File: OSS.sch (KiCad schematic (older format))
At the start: 2 parts, among them U5 27C128

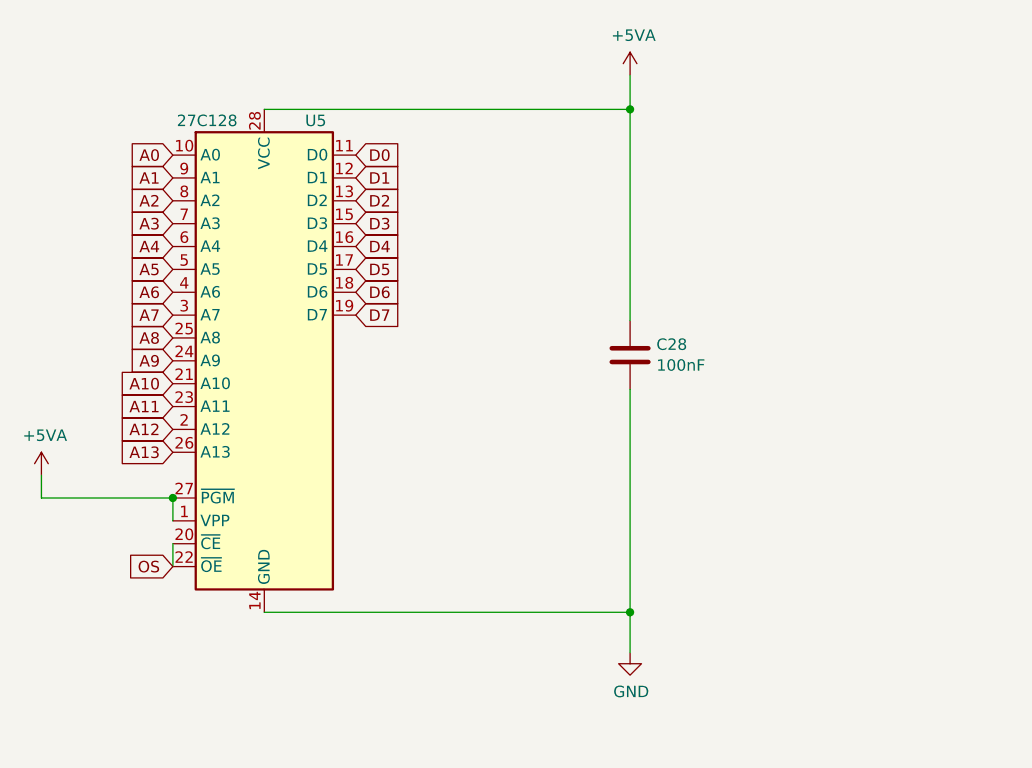
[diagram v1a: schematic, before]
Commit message: OSS and Basic in PLCC
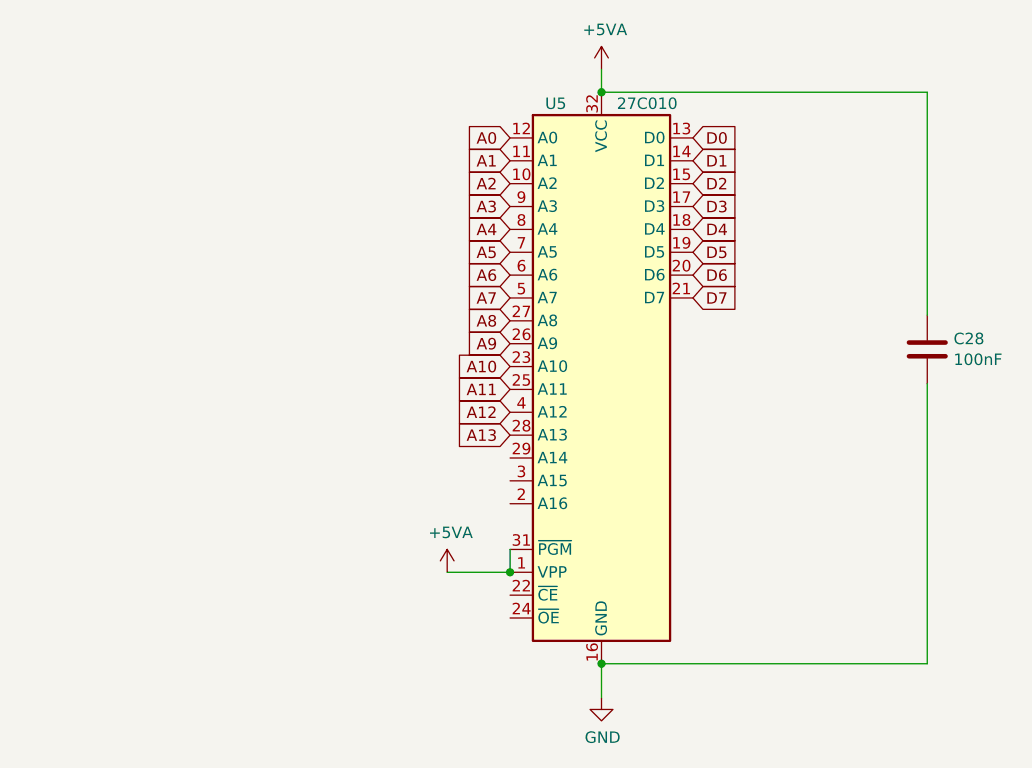
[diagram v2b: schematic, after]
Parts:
- removed U5: 27C128, Package_DIP:DIP-28_W15.24mm_Socket, symbol Memory_EPROM:27C128
- added U5: 27C010, Atari:PLCC-32_THT-Socket, symbol Memory_EPROM:27C010
- C28: footprint Atari:C_Axial_L5.1mm_D2.5mm_P12.50mm_Horizontal -> Capacitor_SMD:C_1206_3216Metric_Pad1.42x1.75mm_HandSolder
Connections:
- net +5VA: now also U5.1 (VPP), U5.31 (~PGM), U5.32 (VCC)
- net A0: now also U5.12 (A0)
- net A1: now also U5.11 (A1)
- net A10: now also U5.23 (A10)
- net A11: now also U5.25 (A11)
- net A12: now also U5.4 (A12)
- net A13: now also U5.28 (A13)
- net A2: now also U5.10 (A2)
- net A3: now also U5.9 (A3)
- net A4: now also U5.8 (A4)
- net A5: now also U5.7 (A5)
- net A6: now also U5.6 (A6)
- net A7: now also U5.5 (A7)
- net A8: now also U5.27 (A8)
- net A9: now also U5.26 (A9)
- net D0: now also U5.13 (D0)
- net D1: now also U5.14 (D1)
- net D2: now also U5.15 (D2)
- net D3: now also U5.17 (D3)
- net D4: now also U5.18 (D4)
- net D5: now also U5.19 (D5)
- net D6: now also U5.20 (D6)
- net D7: now also U5.21 (D7)
- net GND: now also U5.16 (GND)
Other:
- moved on the sheet: C28
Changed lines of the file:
@@
 Comment4 ""
 $EndDescr
-$Comp
-L Memory_EPROM:27C128 U5
-U 1 1 6021796E
-P 5650 3850
-F 0 "U5" H 5875 4900 50  0000 C CNN
-F 1 "27C128" H 5400 4900 50  0000 C CNN
-F 2 "Package_DIP:DIP-28_W15.24mm_Socket" H 5650 3850 50  0001 C CNN
-F 3 "http://ww1.microchip.com/downloads/en/devicedoc/11003L.pdf" H 5650 3850 50  0001 C CNN
-	1    5650 3850
-	1    0    0    -1
-$EndComp
-Text GLabel 5250 2950 0    50   Input ~ 0
+Text GLabel 6725 2875 0    50   Input ~ 0
 A0
-Text GLabel 5250 3050 0    50   Input ~ 0
+Text GLabel 6725 2975 0    50   Input ~ 0
 A1
-Text GLabel 5250 3150 0    50   Input ~ 0
+Text GLabel 6725 3075 0    50   Input ~ 0
 A2
-Text GLabel 5250 3250 0    50   Input ~ 0
+Text GLabel 6725 3175 0    50   Input ~ 0
 A3
-Text GLabel 5250 3350 0    50   Input ~ 0
+Text GLabel 6725 3275 0    50   Input ~ 0
 A4
-Text GLabel 5250 3450 0    50   Input ~ 0
+Text GLabel 6725 3375 0    50   Input ~ 0
 A5
-Text GLabel 5250 3550 0    50   Input ~ 0
+Text GLabel 6725 3475 0    50   Input ~ 0
 A6
-Text GLabel 5250 3650 0    50   Input ~ 0
+Text GLabel 6725 3575 0    50   Input ~ 0
 A7
-Text GLabel 5250 3750 0    50   Input ~ 0
+Text GLabel 6725 3675 0    50   Input ~ 0
 A8
-Text GLabel 5250 3850 0    50   Input ~ 0
+Text GLabel 6725 3775 0    50   Input ~ 0
 A9
-Text GLabel 5250 3950 0    50   Input ~ 0
+Text GLabel 6725 3875 0    50   Input ~ 0
 A10
-Text GLabel 5250 4050 0    50   Input ~ 0
+Text GLabel 6725 3975 0    50   Input ~ 0
 A11
-Text GLabel 5250 4150 0    50   Input ~ 0
+Text GLabel 6725 4075 0    50   Input ~ 0
 A12
-Text GLabel 5250 4250 0    50   Input ~ 0
+Text GLabel 6725 4175 0    50   Input ~ 0
 A13
-Wire Wire Line
-	5250 4450 5250 4550
-Wire Wire Line
-	5250 4650 5250 4750
-Text GLabel 5250 4750 0    50   Input ~ 0
-OS
 $Comp
 L power:+5VA #PWR0149
 U 1 1 60218ED9
-P 4675 4350
-F 0 "#PWR0149" H 4675 4200 50  0001 C CNN
-F 1 "+5VA" H 4690 4523 50  0000 C CNN
-F 2 "" H 4675 4350 50  0001 C CNN
-F 3 "" H 4675 4350 50  0001 C CNN
-	1    4675 4350
+P 6450 4775
+F 0 "#PWR0149" H 6450 4625 50  0001 C CNN
+F 1 "+5VA" H 6465 4948 50  0000 C CNN
+F 2 "" H 6450 4775 50  0001 C CNN
+F 3 "" H 6450 4775 50  0001 C CNN
+	1    6450 4775
 	1    0    0    -1
 $EndComp
-Wire Wire Line
-	5250 4450 4675 4450
-Wire Wire Line
-	4675 4450 4675 4350
-Connection ~ 5250 4450
-Text GLabel 6050 2950 2    50   Input ~ 0
+Text GLabel 7525 2875 2    50   Input ~ 0
 D0
-Text GLabel 6050 3050 2    50   Input ~ 0
+Text GLabel 7525 2975 2    50   Input ~ 0
 D1
-Text GLabel 6050 3150 2    50   Input ~ 0
+Text GLabel 7525 3075 2    50   Input ~ 0
 D2
-Text GLabel 6050 3250 2    50   Input ~ 0
+Text GLabel 7525 3175 2    50   Input ~ 0
 D3
-Text GLabel 6050 3350 2    50   Input ~ 0
+Text GLabel 7525 3275 2    50   Input ~ 0
 D4
-Text GLabel 6050 3450 2    50   Input ~ 0
+Text GLabel 7525 3375 2    50   Input ~ 0
 D5
-Text GLabel 6050 3550 2    50   Input ~ 0
+Text GLabel 7525 3475 2    50   Input ~ 0
 D6
-Text GLabel 6050 3650 2    50   Input ~ 0
+Text GLabel 7525 3575 2    50   Input ~ 0
 D7
 $Comp
 L Device:C C28
 U 1 1 6021A354
-P 7250 3825
-F 0 "C28" H 7365 3871 50  0000 L CNN
-F 1 "100nF" H 7365 3780 50  0000 L CNN
-F 2 "Atari:C_Axial_L5.1mm_D2.5mm_P12.50mm_Horizontal" H 7288 3675 50  0001 C CNN
-F 3 "~" H 7250 3825 50  0001 C CNN
-	1    7250 3825
+P 8550 3800
+F 0 "C28" H 8665 3846 50  0000 L CNN
+F 1 "100nF" H 8665 3755 50  0000 L CNN
+F 2 "Capacitor_SMD:C_1206_3216Metric_Pad1.42x1.75mm_HandSolder" H 8588 3650 50  0001 C CNN
+F 3 "~" H 8550 3800 50  0001 C CNN
+	1    8550 3800
+	1    0    0    -1
+$EndComp
+$Comp
+L power:+5VA #PWR0150
+U 1 1 6021B092
+P 7125 2575
+F 0 "#PWR0150" H 7125 2425 50  0001 C CNN
+F 1 "+5VA" H 7140 2748 50  0000 C CNN
+F 2 "" H 7125 2575 50  0001 C CNN
+F 3 "" H 7125 2575 50  0001 C CNN
+	1    7125 2575
+	1    0    0    -1
+$EndComp
+$Comp
+L power:GND #PWR0151
+U 1 1 6021B848
+P 7125 5325
+F 0 "#PWR0151" H 7125 5075 50  0001 C CNN
+F 1 "GND" H 7130 5152 50  0000 C CNN
+F 2 "" H 7125 5325 50  0001 C CNN
+F 3 "" H 7125 5325 50  0001 C CNN
+	1    7125 5325
+	1    0    0    -1
+$EndComp
+$Comp
+L Memory_EPROM:27C010 U5
+U 1 1 60AAC553
+P 7125 3875
+F 0 "U5" H 6925 5025 50  0000 C CNN
+F 1 "27C010" H 7325 5025 50  0000 C CNN
+F 2 "Atari:PLCC-32_THT-Socket" H 7125 3875 50  0001 C CNN
+F 3 "http://ww1.microchip.com/downloads/en/DeviceDoc/doc0321.pdf" H 7125 3875 50  0001 C CNN
+	1    7125 3875
 	1    0    0    -1
 $EndComp
 Wire Wire Line
-	5650 2750 7250 2750
+	8550 2675 8550 3650
 Wire Wire Line
-	7250 2750 7250 3675
+	8550 3950 8550 5175
 Wire Wire Line
-	5650 4950 7250 4950
+	8550 5175 7125 5175
 Wire Wire Line
-	7250 4950 7250 3975
-$Comp
-L power:+5VA #PWR0150
-U 1 1 6021B092
-P 7250 2600
-F 0 "#PWR0150" H 7250 2450 50  0001 C CNN
-F 1 "+5VA" H 7265 2773 50  0000 C CNN
-F 2 "" H 7250 2600 50  0001 C CNN
-F 3 "" H 7250 2600 50  0001 C CNN
-	1    7250 2600
-	1    0    0    -1
-$EndComp
+	7125 5175 7125 5325
+Connection ~ 7125 5175
 Wire Wire Line
-	7250 2600 7250 2750
-Connection ~ 7250 2750
-$Comp
-L power:GND #PWR0151
-U 1 1 6021B848
-P 7250 5125
-F 0 "#PWR0151" H 7250 4875 50  0001 C CNN
-F 1 "GND" H 7255 4952 50  0000 C CNN
-F 2 "" H 7250 5125 50  0001 C CNN
-F 3 "" H 7250 5125 50  0001 C CNN
-	1    7250 5125
-	1    0    0    -1
-$EndComp
+	7125 2675 8550 2675
 Wire Wire Line
-	7250 5125 7250 4950
-Connection ~ 7250 4950
+	7125 2575 7125 2675
+Connection ~ 7125 2675
+Wire Wire Line
+	6725 4675 6725 4775
+Wire Wire Line
+	6725 4775 6450 4775
+Connection ~ 6725 4775
 $EndSCHEMATC

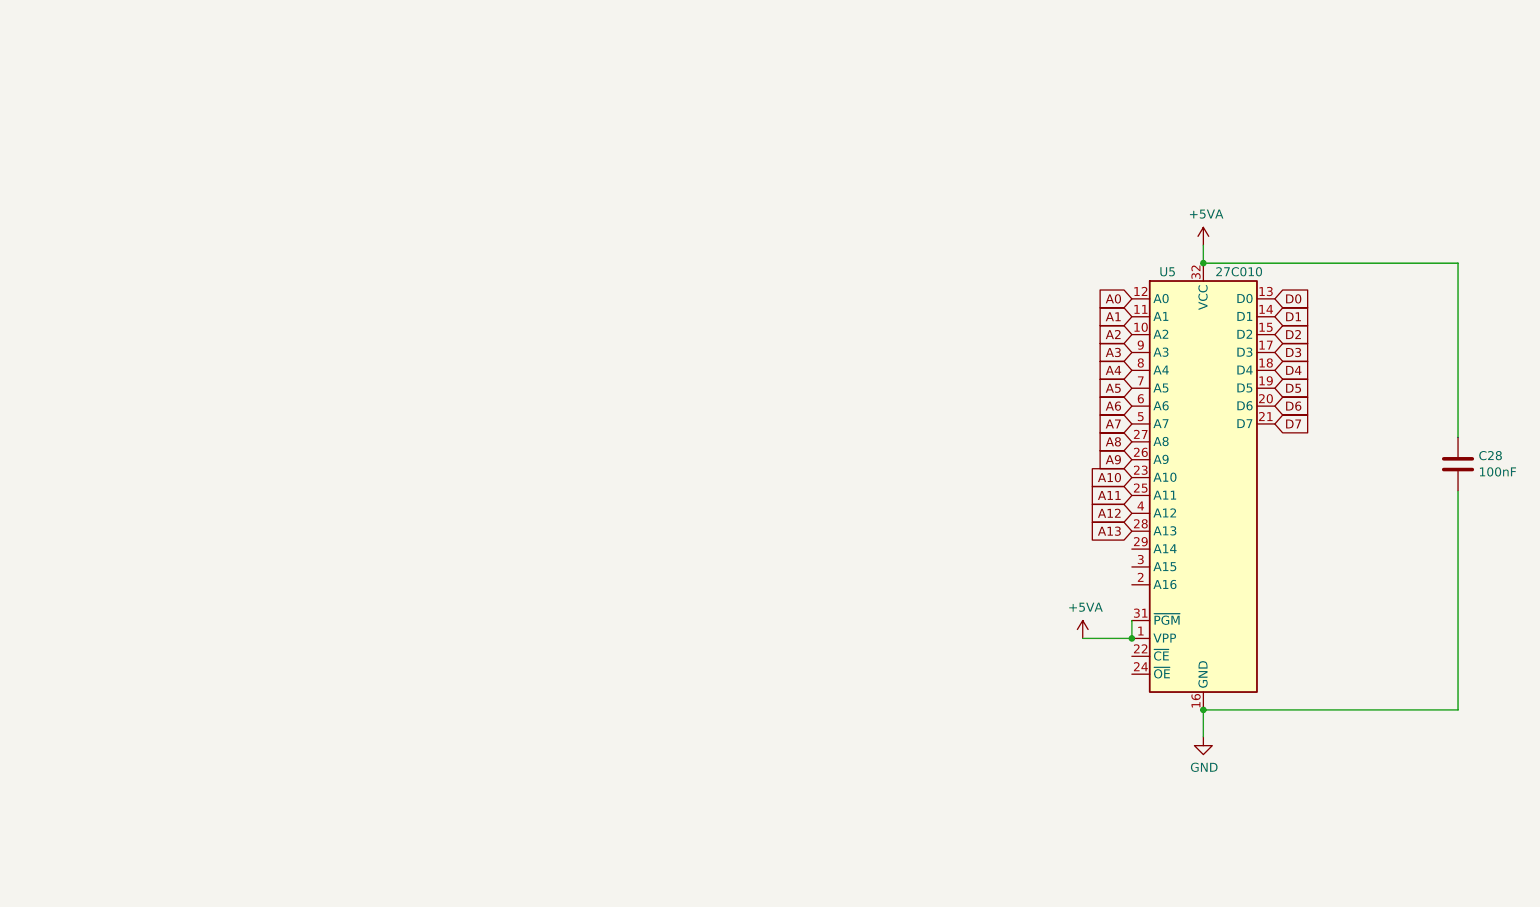
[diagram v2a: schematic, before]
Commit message: Add Basci and SO PLCC
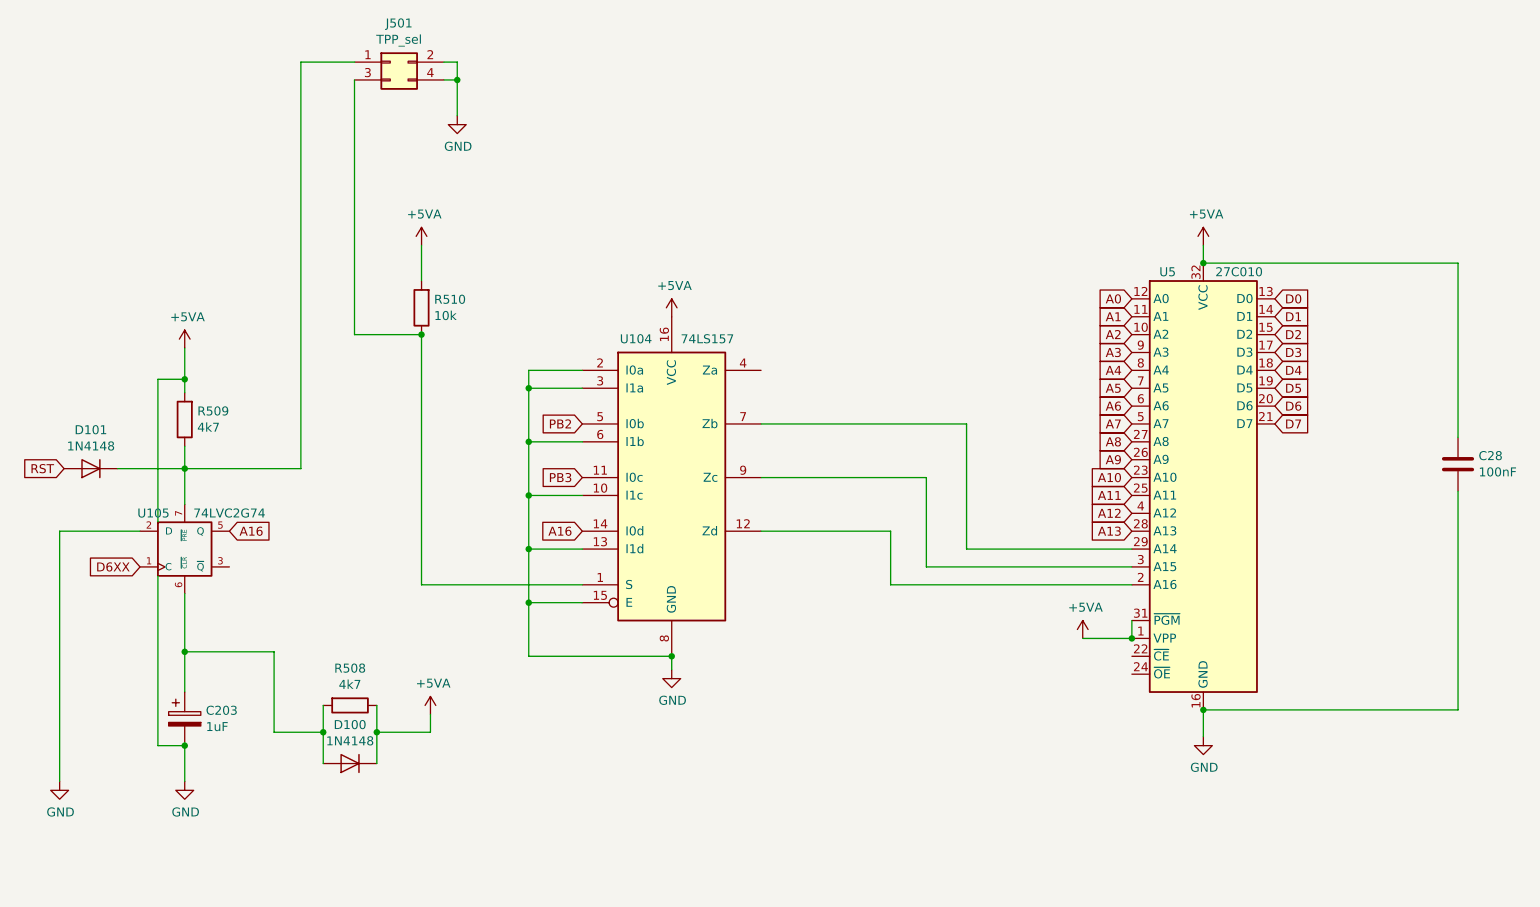
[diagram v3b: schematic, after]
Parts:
- added C203: 1uF, Capacitor_SMD:C_1206_3216Metric_Pad1.42x1.75mm_HandSolder, symbol Device:CP
- added D100, D101: 1N4148, Diode_SMD:D_1206_3216Metric_Pad1.42x1.75mm_HandSolder, symbol Diode:1N4148
- added J501: TPP_sel, Connector_PinHeader_2.54mm:PinHeader_2x02_P2.54mm_Vertical, symbol Connector_Generic:Conn_02x02_Odd_Even
- added R508, R509: 4k7, Resistor_SMD:R_1206_3216Metric_Pad1.42x1.75mm_HandSolder, symbol Device:R
- added R510: 10k, Resistor_SMD:R_1206_3216Metric_Pad1.42x1.75mm_HandSolder, symbol Device:R
- added U104: 74LS157, Package_SO:SOIC-16_3.9x9.9mm_P1.27mm, symbol 74xx:74LS157
- added U105: 74LVC2G74, Package_SO:TSSOP-8_3x3mm_P0.65mm, symbol 74xGxx:74LVC2G74
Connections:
- net +5VA: now also D100.1 (K), R508.1, R509.2, R510.2, U104.16 (VCC), U105.8 (VCC)
- net GND: now also C203.2, J501.2 (Pin_2), J501.4 (Pin_4), U104.10 (I1c), U104.13 (I1d), U104.15 (E), U104.2 (I0a), U104.3 (I1a), U104.6 (I1b), U104.8 (GND), U105.2 (D), U105.4 (GND)
- net at U5.2 (A16): now also U104.12 (Zd)
- net at U5.29 (A14): now also U104.7 (Zb)
- net at U5.3 (A15): now also U104.9 (Zc)
- new net: J501.3 (Pin_3), R510.1, U104.1 (S)
- new net: C203.1, D100.2 (A), R508.2, U105.6 (~CLR)
- new net: D101.1 (K), J501.1 (Pin_1), R509.1, U105.7 (~PRE)
- new net A16: U104.14 (I0d), U105.5 (Q)
- new net D6XX: U105.1 (C)
- new net PB2: U104.5 (I0b)
- new net PB3: U104.11 (I0c)
- new net RST: D101.2 (A)

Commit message: Final modification
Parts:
- added C99: 100nF, Capacitor_SMD:C_1206_3216Metric_Pad1.42x1.75mm_HandSolder, symbol Device:C
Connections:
- net +5VA: now also C99.1
- net A16: now also U104.11 (I0c); no longer U104.14 (I0d)
- net GND: now also U104.14 (I0d), C99.2; no longer U104.2 (I0a)
- net PB3: now also U104.2 (I0a); no longer U104.11 (I0c)
- net at U5.2 (A16): now also U104.9 (Zc); no longer U104.12 (Zd)
- net OS: now reaches U5.22 (~CE)
- net OS: now also U5.24 (~OE)
- net at U5.3 (A15): now also U104.4 (Za); no longer U104.9 (Zc)
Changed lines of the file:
@@
 $EndComp
-Wire Wire Line
-	4650 3575 5800 3575
-Wire Wire Line
-	5800 3575 5800 4275
 Wire Wire Line
 	5800 4275 6725 4275
 Wire Wire Line
-	4650 3875 5575 3875
-Wire Wire Line
-	5575 3875 5575 4375
-Wire Wire Line
 	5575 4375 6725 4375
-Wire Wire Line
-	4650 4175 5375 4175
-Wire Wire Line
-	5375 4175 5375 4475
 Wire Wire Line
 	5375 4475 6725 4475
 Text GLabel 3650 3575 0    50   Input ~ 0
 PB2
+Text GLabel 3650 3275 0    50   Input ~ 0
+PB3
 Text GLabel 3650 3875 0    50   Input ~ 0
-PB3
-Text GLabel 3650 4175 0    50   Input ~ 0
 A16
 $Comp
@@
 	4150 4875 4150 4950
 Wire Wire Line
-	3350 3275 3350 3375
-Wire Wire Line
 	3350 4875 4150 4875
 Connection ~ 4150 4875
 Wire Wire Line
-	3350 3275 3650 3275
-Wire Wire Line
 	3650 3375 3350 3375
-Connection ~ 3350 3375
 Wire Wire Line
 	3350 3375 3350 3675
@@
 Connection ~ 3350 3975
 Wire Wire Line
-	3350 3975 3350 4275
+	3350 3975 3350 4175
 Wire Wire Line
 	3650 4275 3350 4275
@@
 	1    0    0    -1
 $EndComp
-Wire Wire Line
-	1425 3150 1425 3325
 $Comp
 L Diode:1N4148 D101
@@
 Connection ~ 1425 5375
 Wire Wire Line
+	5800 4275 5800 3575
+Wire Wire Line
+	5800 3575 4650 3575
+Wire Wire Line
+	5575 3275 4650 3275
+Wire Wire Line
+	5575 3275 5575 4375
+Wire Wire Line
+	5375 3875 4650 3875
+Wire Wire Line
+	5375 3875 5375 4475
+Wire Wire Line
+	3650 4175 3350 4175
+Connection ~ 3350 4175
+Wire Wire Line
+	3350 4175 3350 4275
+Wire Wire Line
+	6725 4875 6725 4975
+Text GLabel 6500 4975 0    50   Input ~ 0
+OS
+Wire Wire Line
+	6500 4975 6725 4975
+Connection ~ 6725 4975
+Wire Wire Line
 	1275 4125 1275 3325
 Wire Wire Line
+	1425 3325 1425 3400
+Wire Wire Line
+	1425 3150 1425 3325
+Connection ~ 1425 3325
+Wire Wire Line
 	1275 3325 1425 3325
-Connection ~ 1425 3325
-Wire Wire Line
-	1425 3325 1425 3400
+$Comp
+L Device:C C99
+U 1 1 60E536F2
+P 4150 5825
+F 0 "C99" H 4265 5871 50  0000 L CNN
+F 1 "100nF" H 4265 5780 50  0000 L CNN
+F 2 "Capacitor_SMD:C_1206_3216Metric_Pad1.42x1.75mm_HandSolder" H 4188 5675 50  0001 C CNN
+F 3 "~" H 4150 5825 50  0001 C CNN
+	1    4150 5825
+	1    0    0    -1
+$EndComp
+$Comp
+L power:GND #PWR?
+U 1 1 60E543DB
+P 4150 5975
+F 0 "#PWR?" H 4150 5725 50  0001 C CNN
+F 1 "GND" H 4155 5802 50  0000 C CNN
+F 2 "" H 4150 5975 50  0001 C CNN
+F 3 "" H 4150 5975 50  0001 C CNN
+	1    4150 5975
+	1    0    0    -1
+$EndComp
+$Comp
+L power:+5VA #PWR?
+U 1 1 60E5470B
+P 4150 5675
+F 0 "#PWR?" H 4150 5525 50  0001 C CNN
+F 1 "+5VA" H 4165 5848 50  0000 C CNN
+F 2 "" H 4150 5675 50  0001 C CNN
+F 3 "" H 4150 5675 50  0001 C CNN
+	1    4150 5675
+	1    0    0    -1
+$EndComp
 $EndSCHEMATC
